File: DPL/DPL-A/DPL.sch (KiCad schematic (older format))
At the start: 5 parts, among them J3 I2C, U1 SAMD21E, Y1 32.768kHz

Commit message: First prototype of the interstage-balloon release system type A.
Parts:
- renumbered J3 to J2
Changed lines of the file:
@@
 $EndComp
 $Comp
-L Connector:Conn_01x06_Male J3
+L Connector:Conn_01x06_Male J2
 U 1 1 5E277451
 P 6050 3300
-F 0 "J3" H 6158 3679 50  0000 C CNN
+F 0 "J2" H 6158 3679 50  0000 C CNN
 F 1 "I2C" H 6157 3588 50  0000 C CNN
 F 2 "Connector_Molex:Molex_PicoBlade_53048-0610_1x06_P1.25mm_Horizontal" H 6050 3300 50  0001 C CNN

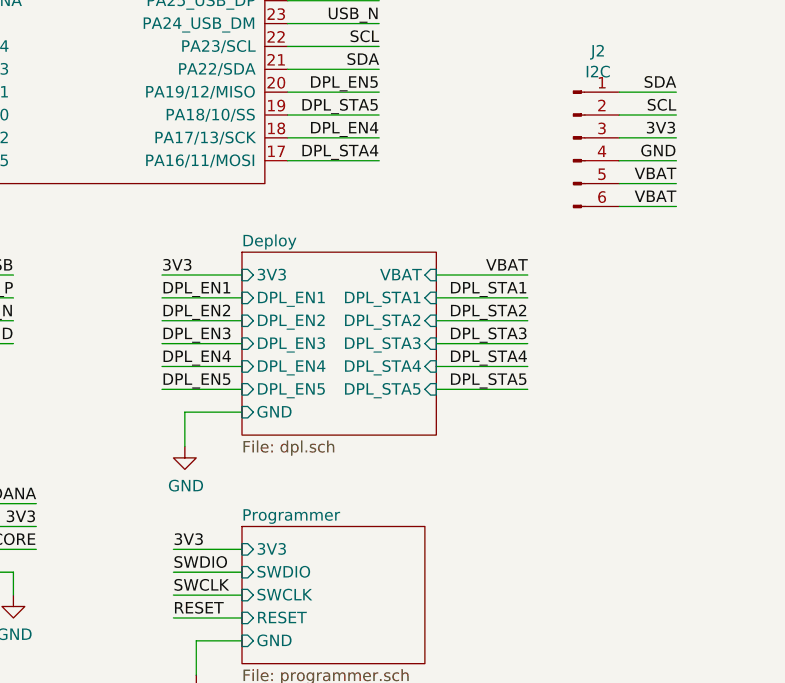
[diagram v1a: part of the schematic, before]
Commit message: Divided the VBAT power line into two independent power lines (VAUX and VAUX2). Changed the schematic and the PCB accordingly. Improved the signal routing. Added an optional resistor to bridge VAUX with VAUX2.
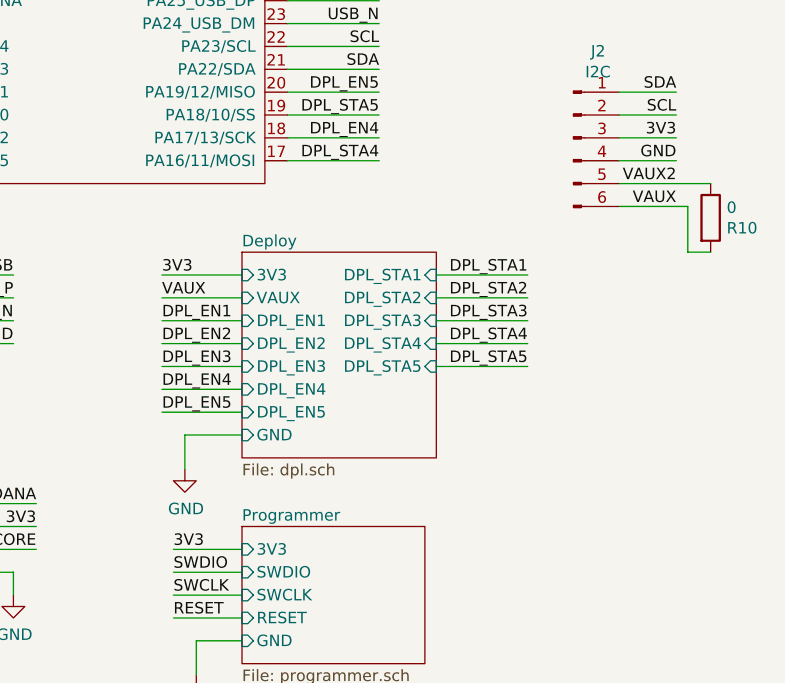
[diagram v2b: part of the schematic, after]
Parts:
- added R10: 0, Resistor_SMD:R_0603_1608Metric_Pad1.05x0.95mm_HandSolder, symbol Device:R
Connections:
- net VBAT renamed VAUX
- net VAUX: now also R10.2; no longer J2.5 (Pin_5)
- new net VAUX2: J2.5 (Pin_5), R10.1
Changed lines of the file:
@@
 	4250 4400 4600 4400
 Wire Wire Line
+	4250 4500 4600 4500
+Wire Wire Line
 	4300 5100 4600 5100
 Wire Wire Line
@@
 	4300 5400 4600 5400
 Wire Wire Line
-	4350 4500 4600 4500
-Wire Wire Line
-	4350 4650 4350 4500
+	4350 4600 4600 4600
+Wire Wire Line
+	4350 4750 4350 4600
 Wire Wire Line
 	4400 5500 4400 5650
@@
 	5450 4300 5850 4300
 Wire Wire Line
-	5450 4400 5850 4400
-Wire Wire Line
 	5850 4200 5450 4200
 Wire Wire Line
@@
 	6250 3400 6500 3400
 Wire Wire Line
-	6250 3500 6500 3500
-Wire Wire Line
-	6250 3600 6500 3600
+	6250 3500 6650 3500
+Wire Wire Line
+	6250 3600 6550 3600
+Wire Wire Line
+	6550 3600 6550 3800
+Wire Wire Line
+	6550 3800 6650 3800
 Text Label 1950 2750 0    50   ~ 0
 GND
@@
 3V3
 Text Label 4250 4000 0    50   ~ 0
+VAUX
+Text Label 4250 4100 0    50   ~ 0
 DPL_EN1
-Text Label 4250 4100 0    50   ~ 0
+Text Label 4250 4200 0    50   ~ 0
 DPL_EN2
-Text Label 4250 4200 0    50   ~ 0
+Text Label 4250 4300 0    50   ~ 0
 DPL_EN3
-Text Label 4250 4300 0    50   ~ 0
+Text Label 4250 4400 0    50   ~ 0
 DPL_EN4
-Text Label 4250 4400 0    50   ~ 0
+Text Label 4250 4500 0    50   ~ 0
 DPL_EN5
 Text Label 4300 5100 0    50   ~ 0
@@
 DPL_STA4
 Text Label 5850 3900 2    50   ~ 0
-VBAT
+DPL_STA1
 Text Label 5850 4000 2    50   ~ 0
-DPL_STA1
+DPL_STA2
 Text Label 5850 4100 2    50   ~ 0
-DPL_STA2
+DPL_STA3
 Text Label 5850 4200 2    50   ~ 0
-DPL_STA3
+DPL_STA4
 Text Label 5850 4300 2    50   ~ 0
-DPL_STA4
-Text Label 5850 4400 2    50   ~ 0
 DPL_STA5
 Text Label 6500 3100 2    50   ~ 0
@@
 GND
 Text Label 6500 3500 2    50   ~ 0
-VBAT
+VAUX2
 Text Label 6500 3600 2    50   ~ 0
-VBAT
+VAUX
 $Comp
 L power:GND #PWR0101
@@
 L power:GND #PWR0111
 U 1 1 5BEB2B09
-P 4350 4650
-F 0 "#PWR0111" H 4350 4400 50  0001 C CNN
-F 1 "GND" H 4355 4477 50  0000 C CNN
-F 2 "" H 4350 4650 50  0001 C CNN
-F 3 "" H 4350 4650 50  0001 C CNN
-	1    4350 4650
+P 4350 4750
+F 0 "#PWR0111" H 4350 4500 50  0001 C CNN
+F 1 "GND" H 4355 4577 50  0000 C CNN
+F 2 "" H 4350 4750 50  0001 C CNN
+F 3 "" H 4350 4750 50  0001 C CNN
+	1    4350 4750
 	1    0    0    -1
 $EndComp
@@
 $EndComp
 $Comp
+L Device:R R10
+U 1 1 5E86F22F
+P 6650 3650
+F 0 "R10" H 6720 3605 50  0000 L CNN
+F 1 "0" H 6720 3695 50  0000 L CNN
+F 2 "Resistor_SMD:R_0603_1608Metric_Pad1.05x0.95mm_HandSolder" V 6580 3650 50  0001 C CNN
+F 3 "~" H 6650 3650 50  0001 C CNN
+	1    6650 3650
+	1    0    0    -1
+$EndComp
+$Comp
 L Device:C Cc1
 U 1 1 5B653719
@@
 $EndComp
 $Sheet
-S 4600 3800 850  800
+S 4600 3800 850  900
 U 5BEF8C81
 F0 "Deploy" 50
 F1 "dpl.sch" 50
-F2 "DPL_EN1" I L 4600 4000 50
-F3 "DPL_EN2" I L 4600 4100 50
-F4 "DPL_EN3" I L 4600 4200 50
-F5 "DPL_EN4" I L 4600 4300 50
+F2 "DPL_EN1" I L 4600 4100 50
+F3 "DPL_EN2" I L 4600 4200 50
+F4 "DPL_EN3" I L 4600 4300 50
+F5 "DPL_EN4" I L 4600 4400 50
 F6 "3V3" I L 4600 3900 50
-F7 "DPL_STA2" I R 5450 4100 50
-F8 "DPL_STA3" I R 5450 4200 50
-F9 "DPL_STA4" I R 5450 4300 50
-F10 "DPL_STA1" I R 5450 4000 50
-F11 "DPL_EN5" I L 4600 4400 50
-F12 "DPL_STA5" I R 5450 4400 50
-F13 "GND" I L 4600 4500 50
-F14 "VBAT" I R 5450 3900 50
+F7 "DPL_STA2" I R 5450 4000 50
+F8 "DPL_STA3" I R 5450 4100 50
+F9 "DPL_STA4" I R 5450 4200 50
+F10 "DPL_STA1" I R 5450 3900 50
+F11 "DPL_EN5" I L 4600 4500 50
+F12 "DPL_STA5" I R 5450 4300 50
+F13 "GND" I L 4600 4600 50
+F14 "VAUX" I L 4600 4000 50
 $EndSheet
 $Sheet
